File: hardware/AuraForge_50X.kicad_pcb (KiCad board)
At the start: 4 copper layers, 100 x 80 mm, 83 parts, among them J1 TYPE-C-31-M-12, J2 PJ-002AH, J3 PJ-320A, J4 Speaker_Left, J5 Speaker_Right, J6 B2B-XH-A, U1 TPA3116D2DAD, U2 TPS61088RHLR, U3 IP2312-4V35, U4 ESP32-WROOM-32E, U5 DW01A-G, U6 FS8205A, U7 AMS1117-3.3

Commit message: Upload updated files.
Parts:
- moved U4 9.69 mm to (26.0, 11.0), turned to -90 degrees
- moved C6 2.00 mm to (6.00, 14.0)
- moved C7 2.00 mm to (6.00, 18.0)
- moved C8 2.00 mm to (6.00, 28.0)
- moved R7 2.00 mm to (6.00, 23.0)
- moved SW_RST1 1.00 mm to (13.5, 36.0)
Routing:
- net /+3V3_SYS: track 129.2 -> 161.8 mm
- net /I2S_LRCK: track 40.9 -> 72.9 mm
- net /I2S_BCK: track 47.0 -> 77.0 mm
- net /ESP_EN: track 29.2 -> 52.9 mm, vias 0 -> 1
- net /ESP_IO0: track 39.7 -> 31.1 mm
- net /ESP_TXD0: track 34.0 -> 42.2 mm
- net /ESP_RXD0: track 33.6 -> 40.0 mm
- net GND: track 150.1 -> 150.9 mm, vias 70 -> 67

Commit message: Upload updated and fixed files.
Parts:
- R9: value 165k 1% -> 91k 1%
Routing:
- net /ESP_EN: track 52.9 -> 47.9 mm, vias 1 -> 0
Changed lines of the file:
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@@
 			)
 		)
-		(property "Value" "165k 1%"
+		(property "Value" "91k 1%"
 			(at 0 1.43 0)
 			(layer "F.Fab")
@@
 	)
 	(segment
+		(start 17.48 33.75)
+		(end 17.48 34)
+		(width 0.15)
+		(layer "F.Cu")
+		(net "/ESP_EN")
+	)
+	(segment
 		(start 7 23)
 		(end 10 20)
@@
 	)
 	(segment
-		(start 17.48 33.75)
-		(end 20.25 33.75)
-		(width 0.15)
-		(layer "F.Cu")
-		(net "/ESP_EN")
-	)
-	(segment
 		(start 6.775 28)
 		(end 6.775 28.775)
@@
 	)
 	(segment
-		(start 20.25 33.75)
-		(end 21 33)
-		(width 0.15)
-		(layer "F.Cu")
-		(net "/ESP_EN")
-	)
-	(segment
 		(start 7 29)
 		(end 7 33)
@@
 		(net "/ESP_EN")
 	)
-	(via
-		(at 21 33)
-		(size 0.6)
-		(drill 0.3)
-		(layers "F.Cu" "B.Cu")
-		(net "/ESP_EN")
-	)
-	(segment
-		(start 21 33)
-		(end 22 32)
-		(width 0.15)
-		(layer "B.Cu")
-		(net "/ESP_EN")
-	)

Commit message: Uploaded latest PCB files.
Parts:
- moved C33 29.8 mm to (89.0, 67.0)
- moved C19 22.2 mm to (84.0, 33.8)
- moved C28 21.0 mm to (77.8, 52.0), turned to 180 degrees
- moved C8 19.7 mm to (14.0, 10.0)
- moved C29 19.0 mm to (84.5, 47.5), turned to 90 degrees
- moved C3 19.0 mm to (38.5, 30.5), turned to 0 degrees
- moved C27 18.8 mm to (74.5, 52.5)
- moved C32 18.6 mm to (73.0, 38.2), turned to 90 degrees
- moved C26 18.2 mm to (71.5, 53.0), turned to 90 degrees
- moved C7 18.1 mm to (14.5, 2.00), turned to -90 degrees
- moved C25 18.1 mm to (69.0, 52.0)
- moved R7 17.5 mm to (13.2, 7.00)
- moved C24 17.1 mm to (66.0, 49.5)
- moved C36 17.1 mm to (94.5, 67.0), turned to 180 degrees
- moved C23 15.9 mm to (67.0, 42.8)
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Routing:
- net Net-(U1-BSPR): track 38.2 -> 3.63 mm
- net Net-(U1-OUTPR): track 40.5 -> 67.8 mm
- net Net-(U1-BSPL): track 30.4 -> 9.22 mm, vias 2 -> 0
- net Net-(U1-LINP): track 22.9 -> 2.90 mm, vias 2 -> 0
- net /SPK_R_MINUS: track 53.4 -> 33.7 mm, vias 2 -> 0
- net Net-(U1-RINN): track 21.8 -> 2.78 mm, vias 2 -> 0
- net Net-(U1-LINN): track 21.8 -> 3.43 mm, vias 2 -> 0
- net Net-(U1-RINP): track 20.7 -> 2.82 mm, vias 2 -> 0
- net /+3V3_SYS: track 161.8 -> 144.3 mm
- net Net-(U1-GVDD): track 25.3 -> 10.1 mm
- net Net-(U1-BSNL): track 24.7 -> 10.9 mm
- net /ESP_EN: track 47.9 -> 38.5 mm
- net /V_LDO_IN: track 30.0 -> 20.9 mm, vias 2 -> 0
- net Net-(U1-OUTPL): track 74.9 -> 83.8 mm
- net /SPK_R_PLUS: track 47.1 -> 38.4 mm, vias 4 -> 0
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
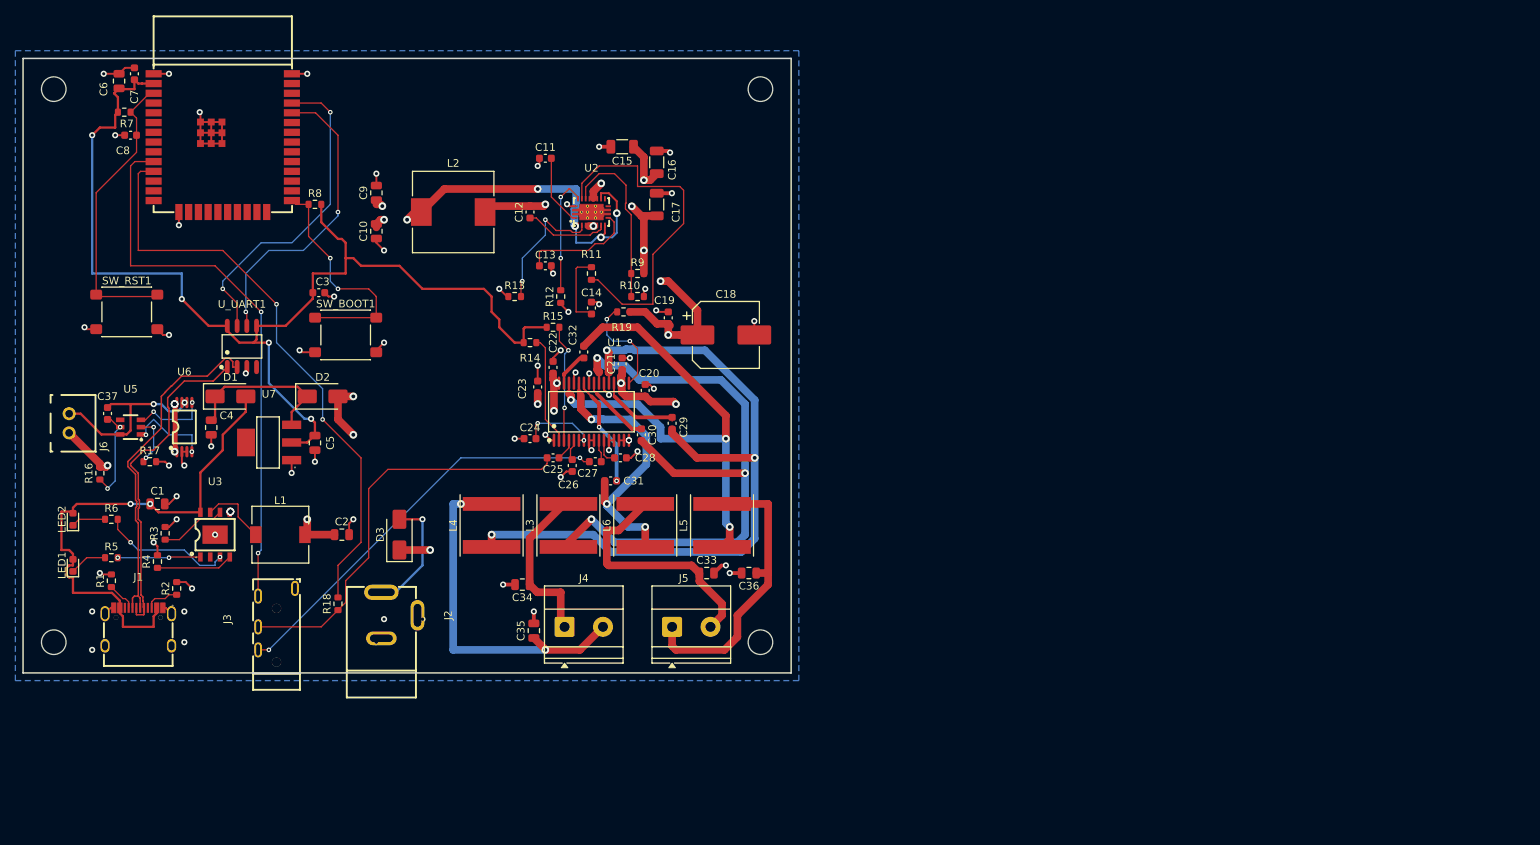
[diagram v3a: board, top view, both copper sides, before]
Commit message: Uploading latest files of New PCB Layout
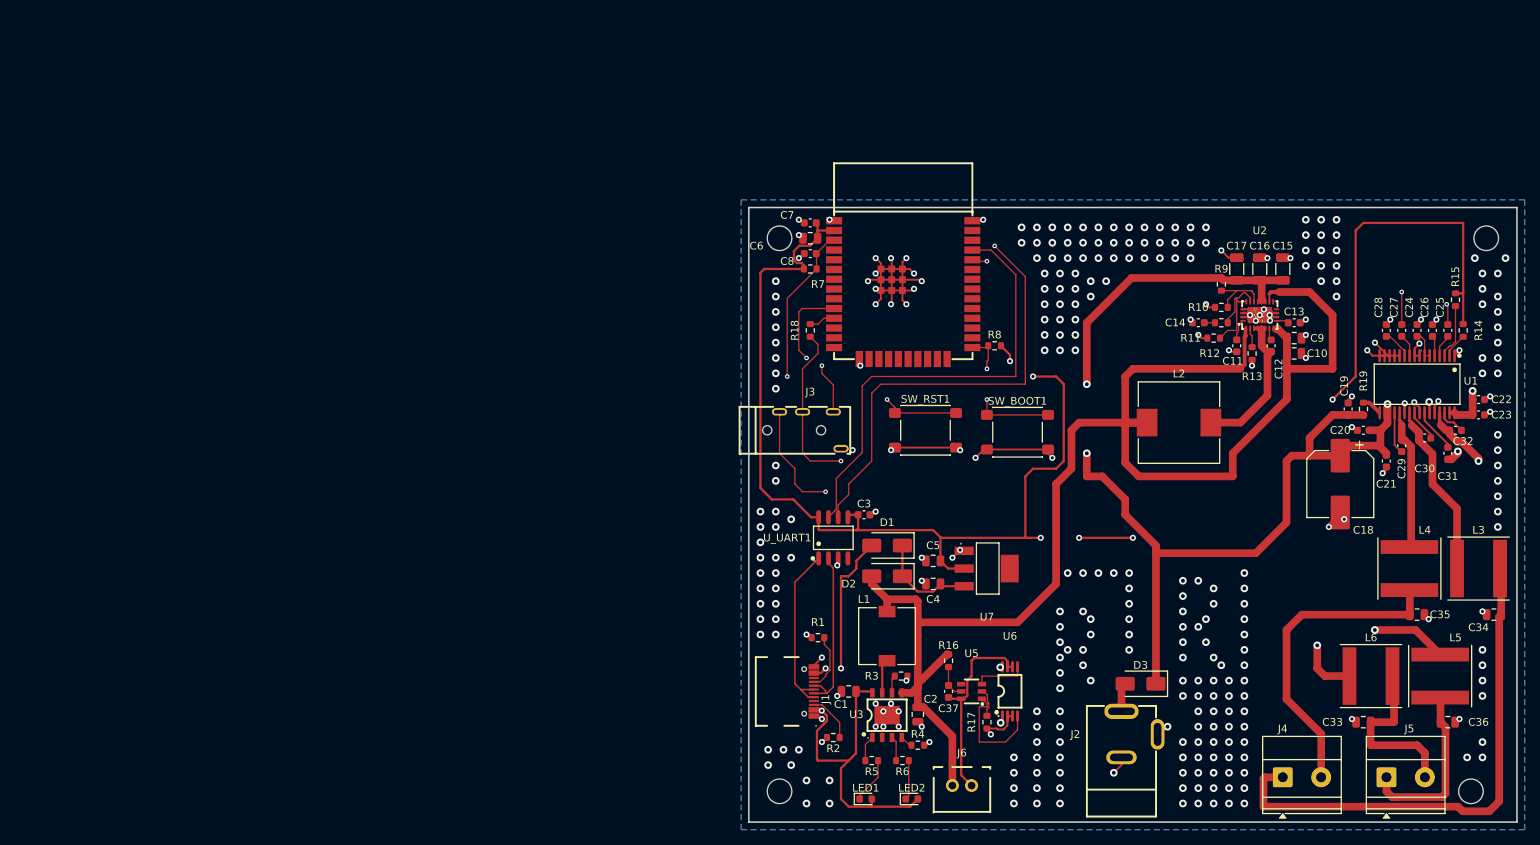
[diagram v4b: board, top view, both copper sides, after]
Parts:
- moved C34 126.5 mm to (191.5, 72.4)
- moved J6 125.4 mm to (122.2, 94.7), turned to 180 degrees
- moved C23 122.5 mm to (189.5, 46.4), turned to 0 degrees
- moved R14 121.5 mm to (187.5, 35.4), turned to -90 degrees
- moved C9 121.0 mm to (165.5, 36.4), turned to 0 degrees
- moved C22 120.6 mm to (189.5, 44.4), turned to 0 degrees
- moved C10 120.5 mm to (165.5, 38.4), turned to 180 degrees
- moved L4 119.6 mm to (180.5, 66.4), turned to -90 degrees
- moved L3 118.6 mm to (189.5, 66.4), turned to 0 degrees
- moved C25 117.7 mm to (185.5, 35.4), turned to -90 degrees
- moved R15 117.5 mm to (186.5, 31.4), turned to -90 degrees
- moved C24 116.3 mm to (181.5, 35.4), turned to -90 degrees
- moved C37 115.3 mm to (120.5, 82.4), turned to 90 degrees
- moved LED2 115.1 mm to (115.7, 96.4), turned to 0 degrees
- moved C35 115.0 mm to (181.5, 72.4), turned to 0 degrees
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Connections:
- net /I2S_BCK renamed /DAC_OUT_R
- net /I2S_LRCK renamed /DAC_OUT_L
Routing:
- net /+3V3_SYS: track 144.3 -> 232.1 mm, vias 4 -> 6
- net /AUDIO_R: track 54.1 -> 138.2 mm, vias 0 -> 2
- net Net-(U1-OUTNL): track 94.2 -> 18.8 mm, vias 3 -> 0
- net /DAC_OUT_R: track 77.0 -> 3.41 mm, vias 2 -> 0
- net /AUDIO_L: track 53.7 -> 120.5 mm
- net Net-(U1-OUTPL): track 83.8 -> 22.8 mm, vias 3 -> 0
- net /DAC_OUT_L: track 72.9 -> 20.2 mm
- net /SPK_L_PLUS: track 22.1 -> 68.0 mm
- net /+BAT_3V7: track 152.1 -> 192.0 mm, vias 14 -> 0
- net Net-(U2-COMP): track 44.9 -> 6.63 mm
- net /+21V_BOOST: track 130.9 -> 161.3 mm, vias 12 -> 4
- net Net-(U1-OUTNR): track 39.5 -> 64.6 mm
- net /USB_DN: track 45.1 -> 22.0 mm
- net /ESP_RXD0: track 39.7 -> 62.5 mm
- net /USB_DP: track 43.3 -> 23.2 mm
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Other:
- outline, holes or cut-outs redrawn

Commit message: Latest PCB files uploaded
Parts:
- L1: footprint Inductor_SMD:L_7.3x7.3_H4.5 -> easyeda2kicad:INDM7066X300N
- L2: footprint Inductor_SMD:L_10.4x10.4_H4.8 -> easyeda2kicad:WE-HCC_8070
- L3, L4, L5, L6: footprint Inductor_SMD:L_Taiyo-Yuden_NR-80xx -> easyeda2kicad:IND_TAIYO_NRS8040_TAY
- moved L5 0.51 mm to (185.0, 80.4)
- moved L4 0.49 mm to (180.0, 66.4)
- moved R3 0.09 mm to (114.3, 80.5)
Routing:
- net /+BAT_3V7: track 192.0 -> 192.7 mm
- net Net-(U3-SW): track 4.44 -> 5.20 mm
- net Net-(U1-OUTNL): track 18.8 -> 19.5 mm
- net Net-(U1-OUTPR): track 56.1 -> 56.6 mm
- net GND: track 157.3 -> 157.7 mm, vias 329 -> 350
